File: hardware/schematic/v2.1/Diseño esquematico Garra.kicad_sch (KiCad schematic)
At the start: 18 parts

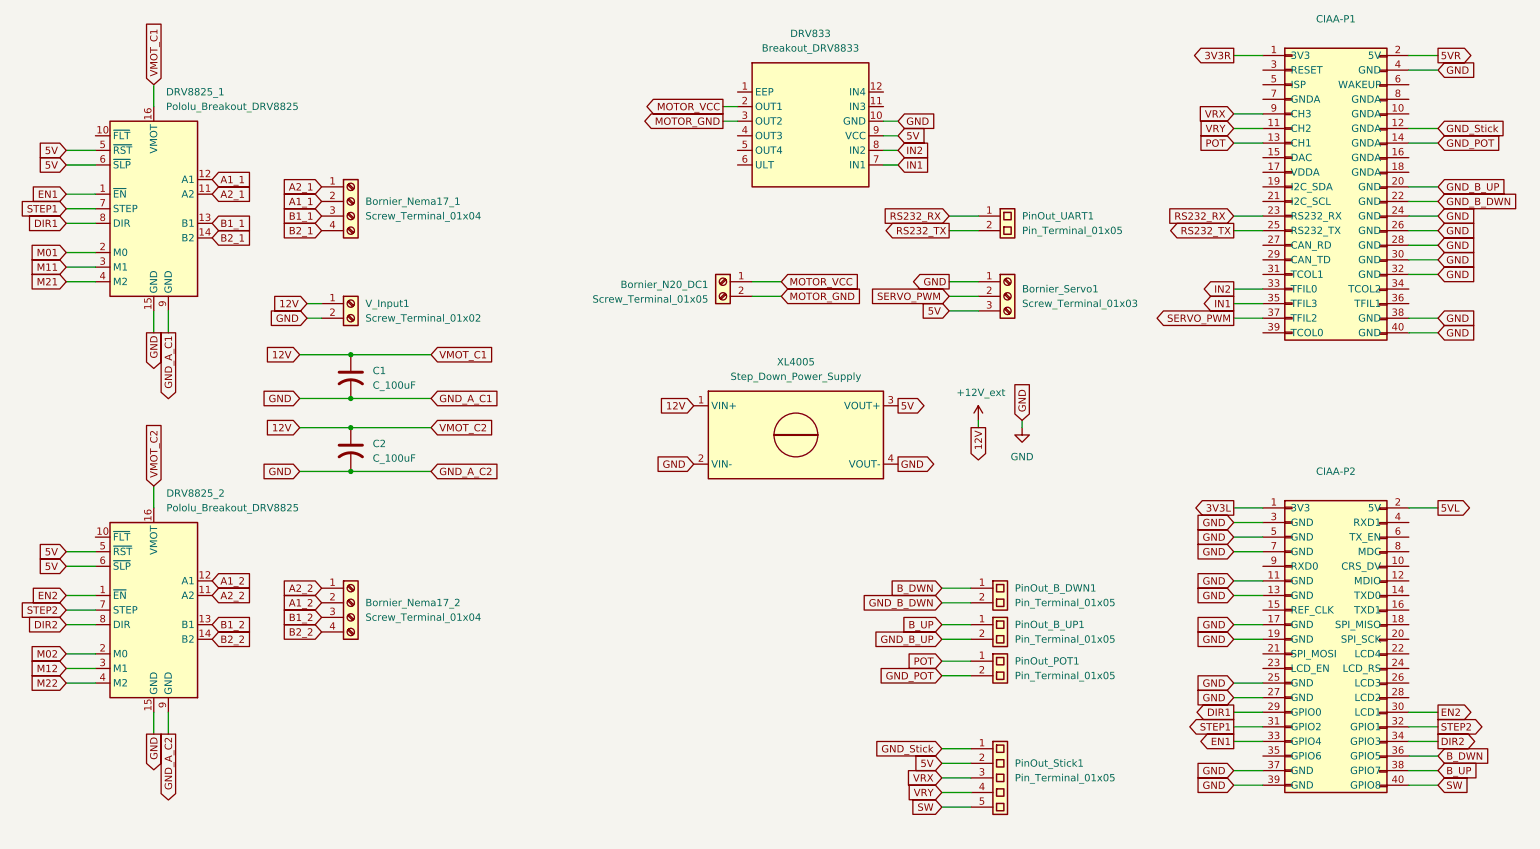
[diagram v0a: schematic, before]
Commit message: feat: add PCB layout (#7)
* refactor

* feat: PCB routing first stage completed

* docs: Schematics PDF added

* fix: PCB border colision

* feat: Copper layers added to the PCB

* feat: New PCB design with new components [LED, B_M]

* feat: add through holes for connectivity & GNDs links

* feat: hole diameter adjustment

* fix: PDF

---------

Co-authored-by: ManuSavenia <saveniamanuel@egmail.com>
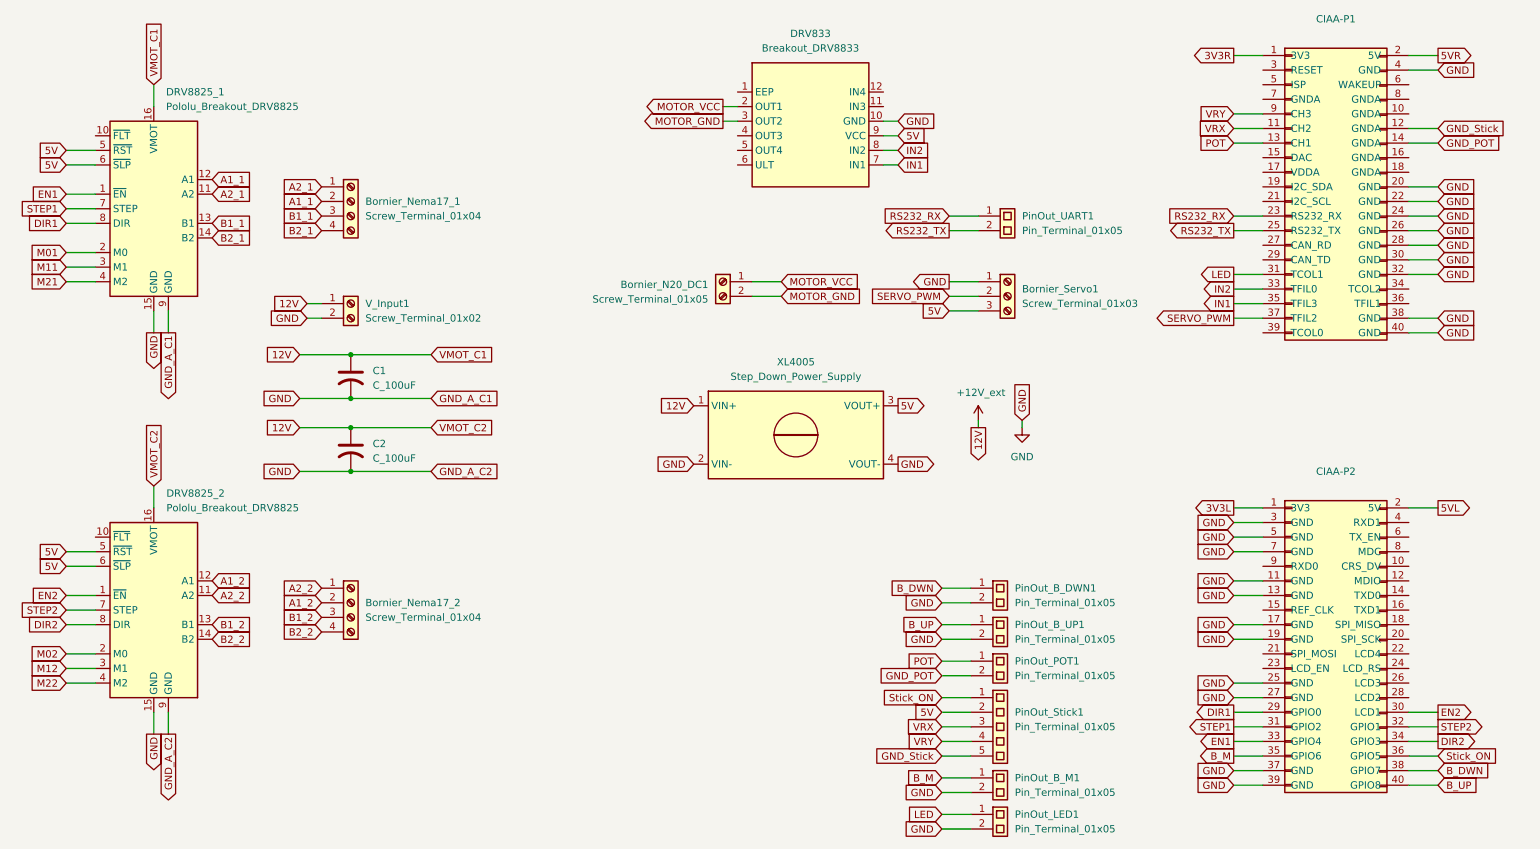
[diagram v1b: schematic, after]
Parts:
- added PinOut_B_M1, PinOut_LED1: Pin_Terminal_01x05, Connector_PinSocket_2.00mm:PinSocket_1x02_P2.00mm_Vertical, symbol Connector:Screw_Terminal_01x02
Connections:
- net GND_B_DWN is gone; now on net GND: CIAA-P1.22 (GND), PinOut_B_DWN1.2 (Pin_2)
- net GND_B_UP is gone; now on net GND: CIAA-P1.20 (GND), PinOut_B_UP1.2 (Pin_2)
- net B_DWN: now also CIAA-P2.38 (GPIO7); no longer CIAA-P2.36 (GPIO5)
- net B_UP: now also CIAA-P2.40 (GPIO8); no longer CIAA-P2.38 (GPIO7)
- net GND: now also PinOut_B_M1.2 (Pin_2), PinOut_LED1.2 (Pin_2)
- net GND_Stick: now also PinOut_Stick1.5 (Pin_5); no longer PinOut_Stick1.1 (Pin_1)
- net VRX: now also CIAA-P1.11 (CH2); no longer CIAA-P1.9 (CH3)
- net VRY: now also CIAA-P1.9 (CH3); no longer CIAA-P1.11 (CH2)
- net LED: now reaches CIAA-P1.31 (TCOL1)
- net LED: now also PinOut_LED1.1 (Pin_1)
- net B_M: now reaches CIAA-P2.35 (GPIO6)
- net B_M: now also PinOut_B_M1.1 (Pin_1)
- removed net SW: CIAA-P2.40 (GPIO8), PinOut_Stick1.5 (Pin_5)
- new net Stick_ON: CIAA-P2.36 (GPIO5), PinOut_Stick1.1 (Pin_1)
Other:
- moved on the sheet: PinOut_Stick1
